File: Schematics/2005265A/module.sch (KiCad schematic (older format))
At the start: 0 parts

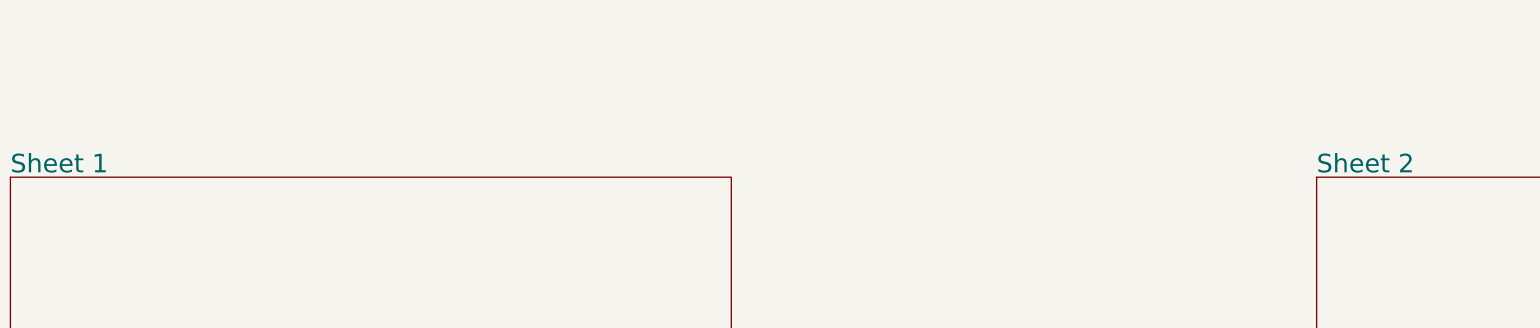
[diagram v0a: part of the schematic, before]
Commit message: Cross-checked and corrected module A15 connector-pad labeling vs pin database.
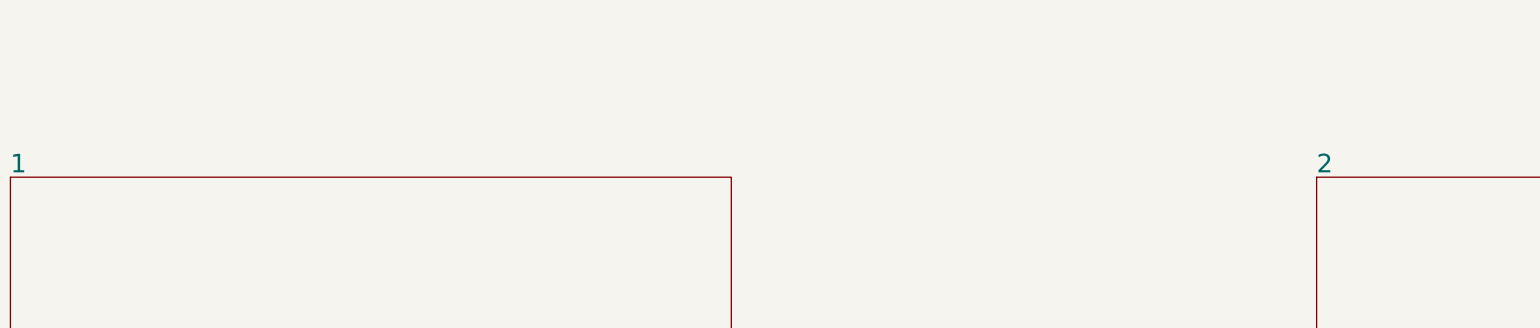
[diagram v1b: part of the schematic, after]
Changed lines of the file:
@@
 S 15250 11550 5450 8975
 U 5B8E7731
-F0 "Sheet 1" 140
+F0 "1" 140
 F1 "2005265A-p1of2.sch" 140
 F2 "0VDCA" U R 20700 17550 140
@@
 S 25125 11550 5450 8975
 U 5B8E7796
-F0 "Sheet 2" 140
+F0 "2" 140
 F1 "2005265A-p2of2.sch" 140
 F2 "0VDCA" U L 25125 17550 140
